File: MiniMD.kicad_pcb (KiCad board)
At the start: 2 copper layers, 100 x 100 mm, 82 parts, among them IC1 A3921KLPTR-T, IC2 SI4900DY-T1-E3, IC3 SI4900DY-T1-E3, IC4 A3921KLPTR-T, IC5 SI4900DY-T1-E3, IC6 SI4900DY-T1-E3, J1 Connector_Generic_Conn_01x05, J2 Connector_Generic_Conn_01x02, J3 Connector_Generic_Conn_01x02, J4 Connector_Generic_Conn_01x05, J5 Connector_Generic_Conn_01x02, J6 Connector_Generic_Conn_01x02, SW1 SW_Push, SW2 SW_Push, U1 FODM217A, U2 FODM217A, U3 FODM217A, U4 FODM217A, U5 FODM217A, U6 FODM217A, U7 FODM217A, U8 FODM217A

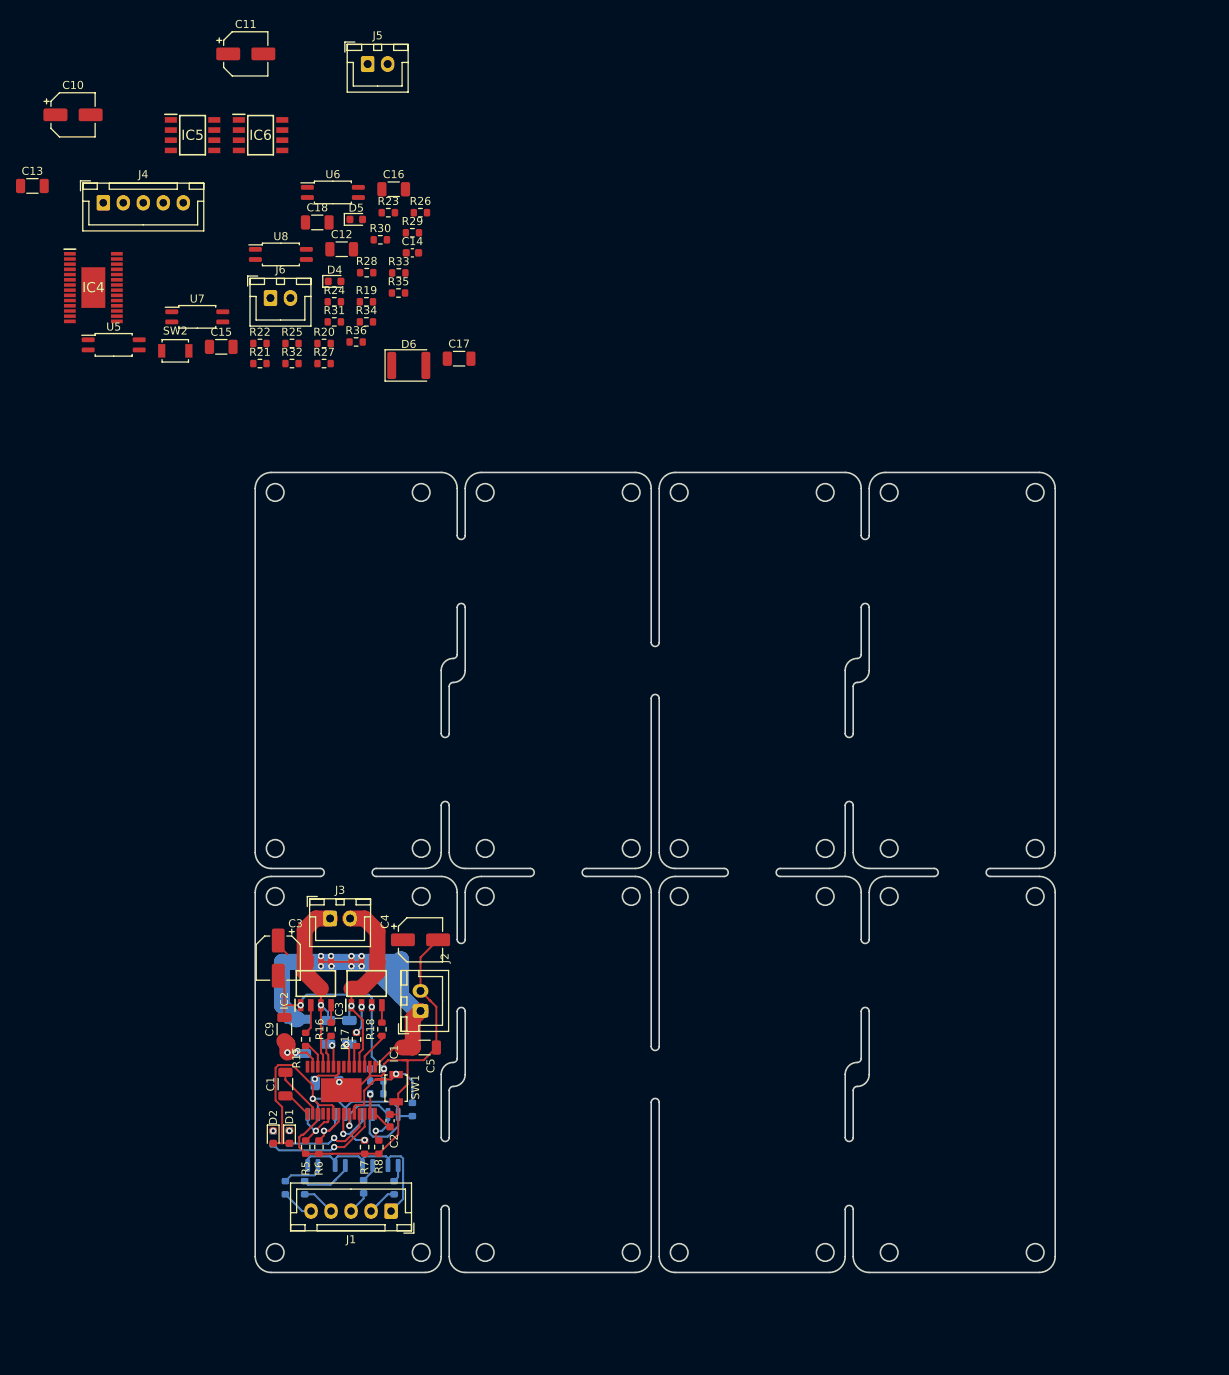
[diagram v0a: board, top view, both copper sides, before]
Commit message: シンボルの挿入まで完成
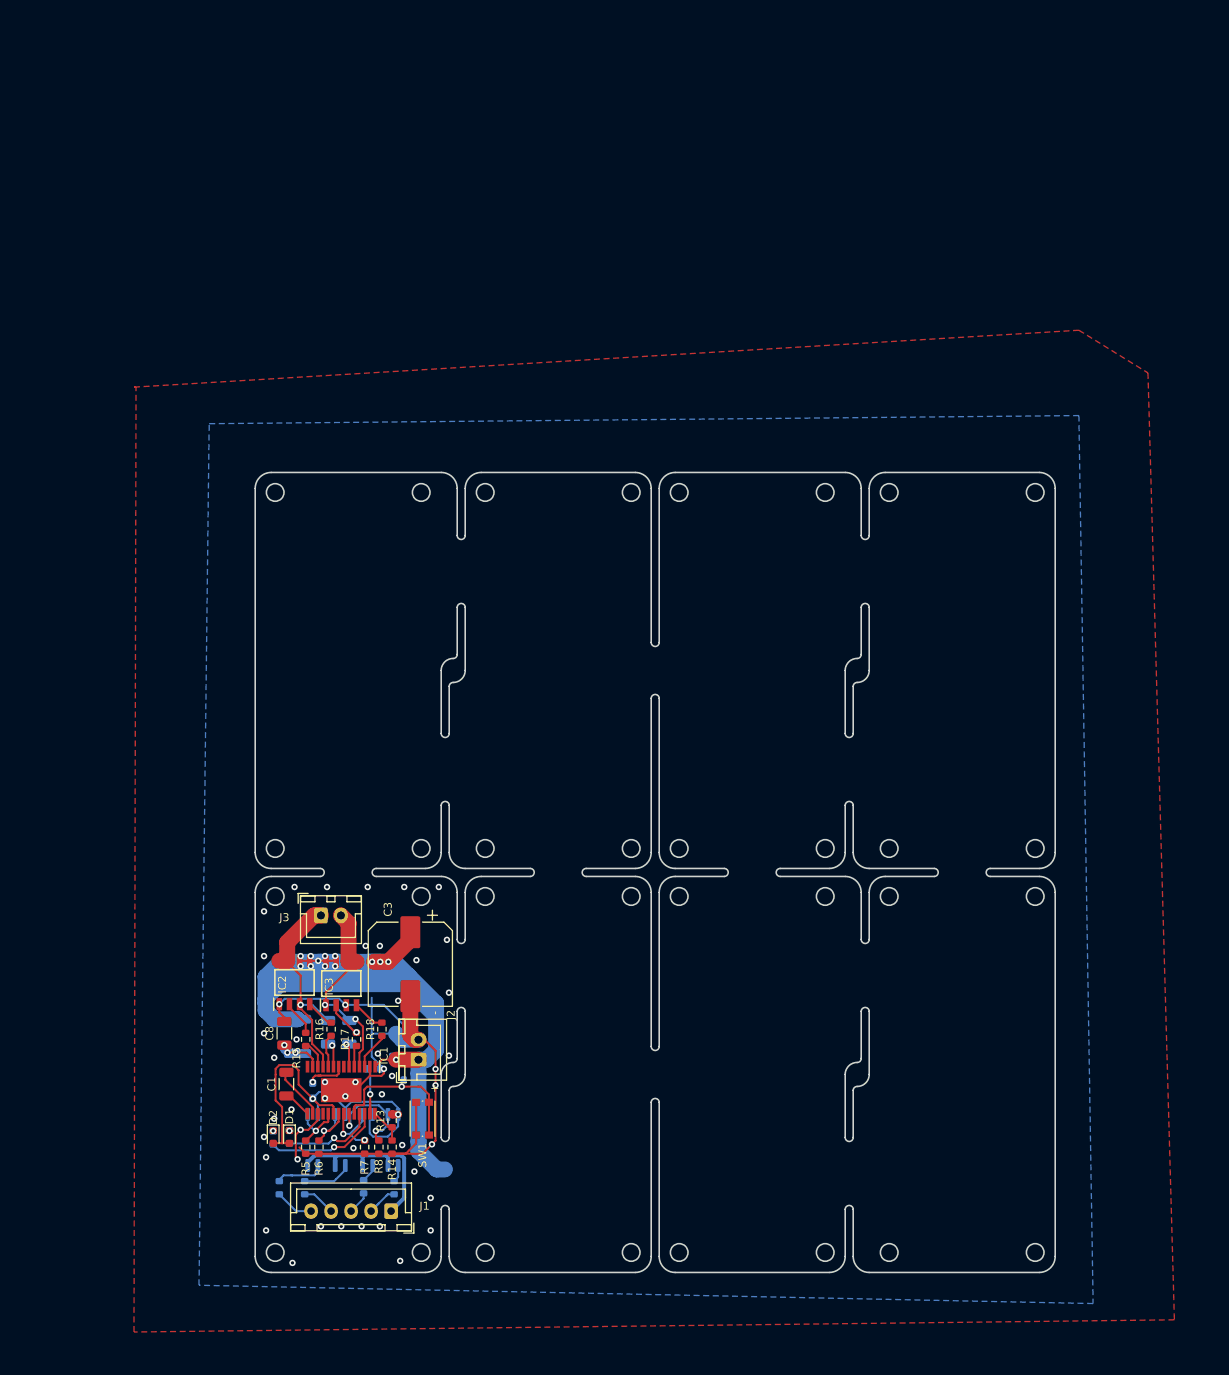
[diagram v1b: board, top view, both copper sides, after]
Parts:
- removed C10, C11: 220u, Capacitor_SMD:CP_Elec_5x3
- removed C12, C13, C17: 0.47u, Capacitor_SMD:C_1206_3216Metric
- removed C14: 0.1u, Capacitor_SMD:C_0603_1608Metric
- removed C15, C16, C18: 0.22u, Capacitor_SMD:C_1206_3216Metric
- removed the C4 at (173.0, 117.1)
- removed D4, D5: LED, LED_SMD:LED_0603_1608Metric
- removed D6: DIODE, Diode_SMD:D_1812_4532Metric
- removed IC4: A3921KLPTR-T, SamacSys_Parts:SOP65P640X120-29N
- removed IC5, IC6: SI4900DY-T1-E3, SamacSys_Parts:SOIC127P600X175-8N
- removed J4: Connector_Generic_Conn_01x05, Connector_JST:JST_XH_B5B-XH-A_1x05_P2.50mm_Vertical
- removed J5, J6: Connector_Generic_Conn_01x02, Connector_JST:JST_XH_B2B-XH-A_1x02_P2.50mm_Vertical
- removed R19, R20, R21, R22, R28, R29, R30, R31, R32: 1k, Resistor_SMD:R_0603_1608Metric
- removed R23, R24, R25, R26, R27: 10k, Resistor_SMD:R_0603_1608Metric
- removed R33, R34, R35, R36: 15, Resistor_SMD:R_0603_1608Metric
- removed SW2: SW_Push, Button_Switch_SMD:SW_SPST_B3U-1000P
- removed U5, U6, U7, U8: FODM217A, Package_SO:SOP-4_4.4x2.6mm_P1.27mm
- C2: value 0.1u -> 1u; moved to B.Cu
- C3: footprint Capacitor_SMD:CP_Elec_5x3 -> Capacitor_SMD:CP_Elec_10x10
- C4: renamed from C5; moved to B.Cu
- C7: renamed from C8; value 0.22u -> 1u; footprint Capacitor_SMD:C_1206_3216Metric -> Capacitor_SMD:C_0603_1608Metric
- R12: value 1k -> 100k
- R13: moved to F.Cu
- R14: value 1k -> 10k; moved to F.Cu
- SW1: value SW_Push -> SW_MEC_5G; footprint Button_Switch_SMD:SW_SPST_B3U-1000P -> Button_Switch_SMD:SW_Push_1P1T_NO_CK_KMR2
- moved C3 16.5 mm to (171.7, 120.1)
- moved C2 9.32 mm to (160.3, 136.9), turned to 0 degrees
- moved R14 6.93 mm to (169.4, 143.0), turned to 270 degrees
- moved J2 6.10 mm to (172.7, 132.1)
- moved R13 5.31 mm to (169.4, 139.7), turned to 90 degrees
- moved SW1 5.04 mm to (173.2, 139.4), turned to 270 degrees
- moved R9 3.69 mm to (171.7, 134.6), turned to 180 degrees
- moved C4 3.57 mm to (169.9, 130.3), turned to 90 degrees
- moved IC3 3.17 mm to (163.1, 122.6)
- moved IC2 2.67 mm to (157.2, 122.4)
- moved J3 1.20 mm to (160.5, 114.0)
- moved C7 1.02 mm to (160.3, 135.0)
- moved R1 0.76 mm to (155.3, 148.1)
- moved C8 0.51 mm to (156.0, 128.8)
- moved R12 0.38 mm to (167.1, 133.2)
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- renumbered C6 to C5, C7 to C6, C9 to C8
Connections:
- C2 pad 1: Net-(C2-Pad1) -> 5V_1
- IC1 pad 28: Net-(C2-Pad1) -> Net-(IC1-Pad28)
- R12 pad 1: Net-(R12-Pad1) -> Net-(IC1-Pad27)
- R13 pad 1: Net-(R12-Pad1) -> Net-(IC1-Pad28)
- R13 pad 2: Net-(R13-Pad2) -> 5V_1
- R14 pad 1: Net-(IC1-Pad27) -> Net-(IC1-Pad28)
- R14 pad 2: Net-(R13-Pad2) -> GND
- R9 pad 1: 5V_1 -> VCC
- SW1 pad 1: GND -> Net-(IC1-Pad24)
- SW1 pad 2: Net-(IC1-Pad24) -> GND
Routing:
- net VCC: track 63.8 -> 124.2 mm, vias 8 -> 13
- net GND: track 89.4 -> 100.8 mm, vias 4 -> 48
- net Net-(C5-Pad2): track 24.5 -> 29.1 mm
- net Net-(IC1-Pad28): track 0.00 -> 4.38 mm
- net Net-(IC1-Pad24): track 15.1 -> 18.8 mm
- net Net-(IC1-Pad27): track 3.88 -> 7.06 mm
- net Net-(C6-Pad2): track 28.5 -> 25.5 mm, vias 1 -> 2
- net Net-(C2-Pad1): track 2.73 -> 0.00 mm
- net Net-(IC3-Pad4): track 2.18 -> 4.08 mm
- net Net-(R13-Pad2): track 1.59 -> 0.00 mm
- net Net-(R12-Pad1): track 1.52 -> 0.00 mm
- net Net-(IC2-Pad4): track 2.18 -> 3.62 mm
- net GND1: track 25.6 -> 24.5 mm
- net Net-(IC3-Pad2): track 3.44 -> 4.56 mm, vias 2 -> 1
- net Net-(R1-Pad2): track 5.35 -> 6.36 mm
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- added copper zone on B.Cu, net GND
- added copper zone on F.Cu, net GND
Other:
- board text added: "+"
- board text added: "-"
- board text added: "GND"
- board text added: "PHASE"
- board text added: "PWMH"
- board text added: "PWML"
- board text added: "SR"
- board text added: "motor"

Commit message: 完成
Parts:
- removed the J1 at (169.3, 151.0)
- removed the R2 at (158.5, 148.1)
- removed the R4 at (169.7, 148.1)
- removed the U2 at (162.9, 142.1)
- removed U4: FODM217A, Package_SO:SOP-4_4.4x2.6mm_P1.27mm
- added C1: 220u, Capacitor_SMD:CP_Elec_10x10, F.Cu at (171.7, 69.6)
- added C1: 220u, Capacitor_SMD:CP_Elec_10x10, F.Cu at (182.5, 97.3)
- added C1: 220u, Capacitor_SMD:CP_Elec_10x10, F.Cu at (222.1, 69.6)
- added C1: 220u, Capacitor_SMD:CP_Elec_10x10, F.Cu at (232.9, 97.3)
- added C1: 220u, Capacitor_SMD:CP_Elec_10x10, F.Cu at (222.1, 120.1)
- added C1: 220u, Capacitor_SMD:CP_Elec_10x10, F.Cu at (232.9, 147.8)
- added C1: 220u, Capacitor_SMD:CP_Elec_10x10, F.Cu at (182.5, 147.8)
- added C2: 0.47u, Capacitor_SMD:C_1206_3216Metric, B.Cu at (169.9, 79.8)
- added C2: 0.47u, Capacitor_SMD:C_1206_3216Metric, B.Cu at (184.3, 87.1)
- added C2: 0.47u, Capacitor_SMD:C_1206_3216Metric, B.Cu at (220.3, 79.8)
- added C2: 0.47u, Capacitor_SMD:C_1206_3216Metric, B.Cu at (234.7, 87.1)
- added C2: 0.47u, Capacitor_SMD:C_1206_3216Metric, B.Cu at (220.3, 130.3)
- added C2: 0.47u, Capacitor_SMD:C_1206_3216Metric, B.Cu at (234.7, 137.7)
- added C2: 0.47u, Capacitor_SMD:C_1206_3216Metric, B.Cu at (184.3, 137.7)
- added C3: 0.47u, Capacitor_SMD:C_1206_3216Metric, F.Cu at (156.0, 78.2)
- added C3: 0.47u, Capacitor_SMD:C_1206_3216Metric, F.Cu at (198.2, 88.6)
- added C3: 0.47u, Capacitor_SMD:C_1206_3216Metric, F.Cu at (206.4, 78.2)
- added C3: 0.47u, Capacitor_SMD:C_1206_3216Metric, F.Cu at (248.7, 88.6)
- added C3: 0.47u, Capacitor_SMD:C_1206_3216Metric, F.Cu at (206.4, 128.8)
- added C3: 0.47u, Capacitor_SMD:C_1206_3216Metric, F.Cu at (248.7, 139.2)
- added C3: 0.47u, Capacitor_SMD:C_1206_3216Metric, F.Cu at (198.2, 139.2)
- added C4: 0.47u, Capacitor_SMD:C_1206_3216Metric, F.Cu at (156.2, 84.6)
- added C4: 0.47u, Capacitor_SMD:C_1206_3216Metric, F.Cu at (198.0, 82.3)
- added C4: 0.47u, Capacitor_SMD:C_1206_3216Metric, F.Cu at (206.6, 84.6)
- added C4: 0.47u, Capacitor_SMD:C_1206_3216Metric, F.Cu at (248.4, 82.3)
- added C4: 0.47u, Capacitor_SMD:C_1206_3216Metric, F.Cu at (206.6, 135.1)
- added C4: 0.47u, Capacitor_SMD:C_1206_3216Metric, F.Cu at (248.4, 132.8)
- added C4: 0.47u, Capacitor_SMD:C_1206_3216Metric, F.Cu at (198.0, 132.8)
- added C5: 0.47u, Capacitor_SMD:C_1206_3216Metric, B.Cu at (161.4, 78.1)
- added C5: 0.47u, Capacitor_SMD:C_1206_3216Metric, B.Cu at (192.8, 88.8)
- added C5: 0.47u, Capacitor_SMD:C_1206_3216Metric, B.Cu at (211.8, 78.1)
- added C5: 0.47u, Capacitor_SMD:C_1206_3216Metric, B.Cu at (243.2, 88.8)
- added C5: 0.47u, Capacitor_SMD:C_1206_3216Metric, B.Cu at (211.8, 128.7)
- added C5: 0.47u, Capacitor_SMD:C_1206_3216Metric, B.Cu at (243.2, 139.3)
- added C5: 0.47u, Capacitor_SMD:C_1206_3216Metric, B.Cu at (192.8, 139.3)
- added C6: 0.47u, Capacitor_SMD:C_1206_3216Metric, B.Cu at (190.1, 88.8)
- added C6: 0.47u, Capacitor_SMD:C_1206_3216Metric, B.Cu at (164.1, 78.1)
- added C6: 0.47u, Capacitor_SMD:C_1206_3216Metric, B.Cu at (240.5, 88.8)
- added C6: 0.47u, Capacitor_SMD:C_1206_3216Metric, B.Cu at (214.5, 78.1)
- added C6: 0.47u, Capacitor_SMD:C_1206_3216Metric, B.Cu at (214.5, 128.7)
- added C6: 0.47u, Capacitor_SMD:C_1206_3216Metric, B.Cu at (240.5, 139.3)
- added C6: 0.47u, Capacitor_SMD:C_1206_3216Metric, B.Cu at (190.1, 139.3)
- added C7: 1u, Capacitor_SMD:C_0603_1608Metric, B.Cu at (160.3, 84.5)
- added C7: 1u, Capacitor_SMD:C_0603_1608Metric, B.Cu at (193.9, 82.4)
- added C7: 1u, Capacitor_SMD:C_0603_1608Metric, B.Cu at (210.7, 84.5)
- added C7: 1u, Capacitor_SMD:C_0603_1608Metric, B.Cu at (244.3, 82.4)
- added C7: 1u, Capacitor_SMD:C_0603_1608Metric, B.Cu at (210.7, 135.0)
- added C7: 1u, Capacitor_SMD:C_0603_1608Metric, B.Cu at (244.3, 133.0)
- added C7: 1u, Capacitor_SMD:C_0603_1608Metric, B.Cu at (193.9, 133.0)
- added C8: 1u, Capacitor_SMD:C_0603_1608Metric, B.Cu at (160.3, 86.4)
- added C8: 1u, Capacitor_SMD:C_0603_1608Metric, B.Cu at (193.9, 80.5)
- added C8: 1u, Capacitor_SMD:C_0603_1608Metric, B.Cu at (210.7, 86.4)
- added C8: 1u, Capacitor_SMD:C_0603_1608Metric, B.Cu at (244.3, 80.5)
- added C8: 1u, Capacitor_SMD:C_0603_1608Metric, B.Cu at (210.7, 136.9)
- added C8: 1u, Capacitor_SMD:C_0603_1608Metric, B.Cu at (244.3, 131.1)
- added C8: 1u, Capacitor_SMD:C_0603_1608Metric, B.Cu at (193.9, 131.1)
- added D1: DIODE, Diode_SMD:D_1812_4532Metric, B.Cu at (157.6, 78.6)
- added D1: DIODE, Diode_SMD:D_1812_4532Metric, B.Cu at (196.6, 88.3)
- added D1: DIODE, Diode_SMD:D_1812_4532Metric, B.Cu at (208.0, 78.6)
- added D1: DIODE, Diode_SMD:D_1812_4532Metric, B.Cu at (247.0, 88.3)
- added D1: DIODE, Diode_SMD:D_1812_4532Metric, B.Cu at (208.0, 129.2)
- added D1: DIODE, Diode_SMD:D_1812_4532Metric, B.Cu at (247.0, 138.8)
- added D1: DIODE, Diode_SMD:D_1812_4532Metric, B.Cu at (196.6, 138.8)
- added D2: LED, LED_SMD:LED_0603_1608Metric, F.Cu at (156.6, 91.2)
- added D2: LED, LED_SMD:LED_0603_1608Metric, F.Cu at (197.6, 75.7)
- added D2: LED, LED_SMD:LED_0603_1608Metric, F.Cu at (207.0, 91.2)
- added D2: LED, LED_SMD:LED_0603_1608Metric, F.Cu at (248.0, 75.7)
- added D2: LED, LED_SMD:LED_0603_1608Metric, F.Cu at (207.0, 141.7)
- added D2: LED, LED_SMD:LED_0603_1608Metric, F.Cu at (248.0, 126.2)
- added D2: LED, LED_SMD:LED_0603_1608Metric, F.Cu at (197.6, 126.2)
- added D3: LED, LED_SMD:LED_0603_1608Metric, F.Cu at (154.6, 91.2)
- added D3: LED, LED_SMD:LED_0603_1608Metric, F.Cu at (199.6, 75.7)
- added D3: LED, LED_SMD:LED_0603_1608Metric, F.Cu at (205.0, 91.2)
- added D3: LED, LED_SMD:LED_0603_1608Metric, F.Cu at (250.1, 75.7)
- added D3: LED, LED_SMD:LED_0603_1608Metric, F.Cu at (205.0, 141.7)
- added D3: LED, LED_SMD:LED_0603_1608Metric, F.Cu at (250.1, 126.2)
- added D3: LED, LED_SMD:LED_0603_1608Metric, F.Cu at (199.6, 126.2)
- added G***: LOGO, MyLibrary:my_symbol_m, B.Cu at (171.7, 93.0)
- added G***: LOGO, MyLibrary:my_symbol_m, B.Cu at (182.5, 73.9)
- added G***: LOGO, MyLibrary:my_symbol_m, B.Cu at (222.1, 93.0)
- added G***: LOGO, MyLibrary:my_symbol_m, B.Cu at (232.9, 73.9)
- added G***: LOGO, MyLibrary:my_symbol_m, B.Cu at (222.1, 143.5)
- added G***: LOGO, MyLibrary:my_symbol_m, B.Cu at (232.9, 124.5)
- added G***: LOGO, MyLibrary:my_symbol_m, B.Cu at (182.5, 124.5)
- added G***: LOGO, MyLibrary:my_symbol_m, B.Cu at (171.7, 143.5)
- added IC1: SI4900DY-T1-E3, SamacSys_Parts:SOIC127P600X175-8N, F.Cu at (197.0, 145.5)
- added IC1: SI4900DY-T1-E3, SamacSys_Parts:SOIC127P600X175-8N, F.Cu at (207.6, 122.4)
- added IC1: SI4900DY-T1-E3, SamacSys_Parts:SOIC127P600X175-8N, F.Cu at (247.4, 145.5)
- added IC1: SI4900DY-T1-E3, SamacSys_Parts:SOIC127P600X175-8N, F.Cu at (247.4, 95.0)
- added IC1: SI4900DY-T1-E3, SamacSys_Parts:SOIC127P600X175-8N, F.Cu at (207.6, 71.9)
- added IC1: SI4900DY-T1-E3, SamacSys_Parts:SOIC127P600X175-8N, F.Cu at (197.0, 95.0)
- added IC1: SI4900DY-T1-E3, SamacSys_Parts:SOIC127P600X175-8N, F.Cu at (157.2, 71.9)
- added IC2: SI4900DY-T1-E3, SamacSys_Parts:SOIC127P600X175-8N, F.Cu at (191.1, 145.4)
- added IC2: SI4900DY-T1-E3, SamacSys_Parts:SOIC127P600X175-8N, F.Cu at (213.5, 122.6)
- added IC2: SI4900DY-T1-E3, SamacSys_Parts:SOIC127P600X175-8N, F.Cu at (241.6, 145.4)
- added IC2: SI4900DY-T1-E3, SamacSys_Parts:SOIC127P600X175-8N, F.Cu at (241.6, 94.9)
- added IC2: SI4900DY-T1-E3, SamacSys_Parts:SOIC127P600X175-8N, F.Cu at (213.5, 72.0)
- added IC2: SI4900DY-T1-E3, SamacSys_Parts:SOIC127P600X175-8N, F.Cu at (191.1, 94.9)
- added IC2: SI4900DY-T1-E3, SamacSys_Parts:SOIC127P600X175-8N, F.Cu at (163.1, 72.0)
- added IC3: A3921KLPTR-T, SamacSys_Parts:SOP65P640X120-29N, F.Cu at (191.1, 132.1)
- added IC3: A3921KLPTR-T, SamacSys_Parts:SOP65P640X120-29N, F.Cu at (213.5, 135.9)
- added IC3: A3921KLPTR-T, SamacSys_Parts:SOP65P640X120-29N, F.Cu at (241.6, 132.1)
- added IC3: A3921KLPTR-T, SamacSys_Parts:SOP65P640X120-29N, F.Cu at (241.6, 81.5)
- added IC3: A3921KLPTR-T, SamacSys_Parts:SOP65P640X120-29N, F.Cu at (213.5, 85.3)
- added IC3: A3921KLPTR-T, SamacSys_Parts:SOP65P640X120-29N, F.Cu at (191.1, 81.5)
- added IC3: A3921KLPTR-T, SamacSys_Parts:SOP65P640X120-29N, F.Cu at (163.1, 85.3)
- added J1: Connector_Generic_Conn_01x02, Connector_JST:JST_XH_B2B-XH-A_1x02_P2.50mm_Vertical, F.Cu at (172.7, 81.5)
- added J1: Connector_Generic_Conn_01x02, Connector_JST:JST_XH_B2B-XH-A_1x02_P2.50mm_Vertical, F.Cu at (181.5, 85.3)
- added J1: Connector_Generic_Conn_01x02, Connector_JST:JST_XH_B2B-XH-A_1x02_P2.50mm_Vertical, F.Cu at (223.1, 81.5)
- added J1: Connector_Generic_Conn_01x02, Connector_JST:JST_XH_B2B-XH-A_1x02_P2.50mm_Vertical, F.Cu at (231.9, 85.3)
- added J1: Connector_Generic_Conn_01x02, Connector_JST:JST_XH_B2B-XH-A_1x02_P2.50mm_Vertical, F.Cu at (223.1, 132.1)
- added J1: Connector_Generic_Conn_01x02, Connector_JST:JST_XH_B2B-XH-A_1x02_P2.50mm_Vertical, F.Cu at (231.9, 135.9)
- added J1: Connector_Generic_Conn_01x02, Connector_JST:JST_XH_B2B-XH-A_1x02_P2.50mm_Vertical, F.Cu at (181.5, 135.9)
- added J2: Conn_01x03, Connector_JST:JST_XH_B3B-XH-A_1x03_P2.50mm_Vertical, F.Cu at (162.0, 100.5)
- added J2: Conn_01x03, Connector_JST:JST_XH_B3B-XH-A_1x03_P2.50mm_Vertical, F.Cu at (192.2, 66.4)
- added J2: Conn_01x03, Connector_JST:JST_XH_B3B-XH-A_1x03_P2.50mm_Vertical, F.Cu at (212.4, 100.5)
- added J2: Conn_01x03, Connector_JST:JST_XH_B3B-XH-A_1x03_P2.50mm_Vertical, F.Cu at (242.6, 66.4)
- added J2: Conn_01x03, Connector_JST:JST_XH_B3B-XH-A_1x03_P2.50mm_Vertical, F.Cu at (212.4, 151.0)
- added J2: Conn_01x03, Connector_JST:JST_XH_B3B-XH-A_1x03_P2.50mm_Vertical, F.Cu at (242.6, 117.0)
- added J2: Conn_01x03, Connector_JST:JST_XH_B3B-XH-A_1x03_P2.50mm_Vertical, F.Cu at (192.2, 117.0)
- added J2: Conn_01x03, Connector_JST:JST_XH_B3B-XH-A_1x03_P2.50mm_Vertical, F.Cu at (162.0, 151.0)
- added J3: Connector_Generic_Conn_01x02, Connector_JST:JST_XH_B2B-XH-A_1x02_P2.50mm_Vertical, F.Cu at (191.0, 103.3)
- added J3: Connector_Generic_Conn_01x02, Connector_JST:JST_XH_B2B-XH-A_1x02_P2.50mm_Vertical, F.Cu at (163.2, 63.6)
- added J3: Connector_Generic_Conn_01x02, Connector_JST:JST_XH_B2B-XH-A_1x02_P2.50mm_Vertical, F.Cu at (213.6, 63.6)
- added J3: Connector_Generic_Conn_01x02, Connector_JST:JST_XH_B2B-XH-A_1x02_P2.50mm_Vertical, F.Cu at (241.4, 103.3)
- added J3: Connector_Generic_Conn_01x02, Connector_JST:JST_XH_B2B-XH-A_1x02_P2.50mm_Vertical, F.Cu at (213.6, 114.2)
- added J3: Connector_Generic_Conn_01x02, Connector_JST:JST_XH_B2B-XH-A_1x02_P2.50mm_Vertical, F.Cu at (241.4, 153.8)
- added J3: Connector_Generic_Conn_01x02, Connector_JST:JST_XH_B2B-XH-A_1x02_P2.50mm_Vertical, F.Cu at (191.0, 153.8)
- added R1: 10k, Resistor_SMD:R_0603_1608Metric, B.Cu at (171.7, 84.1)
- added R1: 10k, Resistor_SMD:R_0603_1608Metric, B.Cu at (182.5, 82.8)
- added R1: 10k, Resistor_SMD:R_0603_1608Metric, B.Cu at (222.1, 84.1)
- added R1: 10k, Resistor_SMD:R_0603_1608Metric, B.Cu at (232.9, 82.8)
- added R1: 10k, Resistor_SMD:R_0603_1608Metric, B.Cu at (222.1, 134.6)
- added R1: 10k, Resistor_SMD:R_0603_1608Metric, B.Cu at (232.9, 133.3)
- added R1: 10k, Resistor_SMD:R_0603_1608Metric, B.Cu at (182.5, 133.3)
- added R10: 10k, Resistor_SMD:R_0603_1608Metric, F.Cu at (166.0, 92.5)
- added R10: 10k, Resistor_SMD:R_0603_1608Metric, F.Cu at (188.2, 74.4)
- added R10: 10k, Resistor_SMD:R_0603_1608Metric, F.Cu at (216.4, 92.5)
- added R10: 10k, Resistor_SMD:R_0603_1608Metric, F.Cu at (238.6, 74.4)
- added R10: 10k, Resistor_SMD:R_0603_1608Metric, F.Cu at (216.4, 143.0)
- added R10: 10k, Resistor_SMD:R_0603_1608Metric, F.Cu at (238.6, 125.0)
- added R10: 10k, Resistor_SMD:R_0603_1608Metric, F.Cu at (188.2, 125.0)
- added R11: 47, Resistor_SMD:R_0603_1608Metric, F.Cu at (168.1, 77.7)
- added R11: 47, Resistor_SMD:R_0603_1608Metric, F.Cu at (186.1, 89.2)
- added R11: 47, Resistor_SMD:R_0603_1608Metric, F.Cu at (218.6, 77.7)
- added R11: 47, Resistor_SMD:R_0603_1608Metric, F.Cu at (236.5, 89.2)
- added R11: 47, Resistor_SMD:R_0603_1608Metric, F.Cu at (218.6, 128.3)
- added R11: 47, Resistor_SMD:R_0603_1608Metric, F.Cu at (236.5, 139.7)
- added R11: 47, Resistor_SMD:R_0603_1608Metric, F.Cu at (186.1, 139.7)
- added R12: 1k, Resistor_SMD:R_0603_1608Metric, B.Cu at (156.6, 91.2)
- added R12: 1k, Resistor_SMD:R_0603_1608Metric, B.Cu at (197.6, 75.7)
- added R12: 1k, Resistor_SMD:R_0603_1608Metric, B.Cu at (207.0, 91.2)
- added R12: 1k, Resistor_SMD:R_0603_1608Metric, B.Cu at (248.0, 75.7)
- added R12: 1k, Resistor_SMD:R_0603_1608Metric, B.Cu at (207.0, 141.7)
- added R12: 1k, Resistor_SMD:R_0603_1608Metric, B.Cu at (248.0, 126.2)
- added R12: 1k, Resistor_SMD:R_0603_1608Metric, B.Cu at (197.6, 126.2)
- added R13: 1k, Resistor_SMD:R_0603_1608Metric, B.Cu at (154.6, 91.3)
- added R13: 1k, Resistor_SMD:R_0603_1608Metric, B.Cu at (199.6, 75.6)
- added R13: 1k, Resistor_SMD:R_0603_1608Metric, B.Cu at (205.0, 91.3)
- added R13: 1k, Resistor_SMD:R_0603_1608Metric, B.Cu at (250.1, 75.6)
- added R13: 1k, Resistor_SMD:R_0603_1608Metric, B.Cu at (205.0, 141.9)
- added R13: 1k, Resistor_SMD:R_0603_1608Metric, B.Cu at (250.1, 126.1)
- added R13: 1k, Resistor_SMD:R_0603_1608Metric, B.Cu at (199.6, 126.1)
- added R14: 100k, Resistor_SMD:R_0603_1608Metric, B.Cu at (167.1, 82.7)
- added R14: 100k, Resistor_SMD:R_0603_1608Metric, B.Cu at (187.1, 84.2)
- added R14: 100k, Resistor_SMD:R_0603_1608Metric, B.Cu at (217.6, 82.7)
- added R14: 100k, Resistor_SMD:R_0603_1608Metric, B.Cu at (237.5, 84.2)
- added R14: 100k, Resistor_SMD:R_0603_1608Metric, B.Cu at (217.6, 133.2)
- added R14: 100k, Resistor_SMD:R_0603_1608Metric, B.Cu at (237.5, 134.7)
- added R14: 100k, Resistor_SMD:R_0603_1608Metric, B.Cu at (187.1, 134.7)
- added R15: 1k, Resistor_SMD:R_0603_1608Metric, F.Cu at (169.4, 89.2)
- added R15: 1k, Resistor_SMD:R_0603_1608Metric, F.Cu at (184.8, 77.7)
- added R15: 1k, Resistor_SMD:R_0603_1608Metric, F.Cu at (219.8, 89.2)
- added R15: 1k, Resistor_SMD:R_0603_1608Metric, F.Cu at (235.2, 77.7)
- added R15: 1k, Resistor_SMD:R_0603_1608Metric, F.Cu at (219.8, 139.7)
- added R15: 1k, Resistor_SMD:R_0603_1608Metric, F.Cu at (235.2, 128.3)
- added R15: 1k, Resistor_SMD:R_0603_1608Metric, F.Cu at (184.8, 128.3)
- added R16: 10k, Resistor_SMD:R_0603_1608Metric, F.Cu at (184.8, 74.4)
- added R16: 10k, Resistor_SMD:R_0603_1608Metric, F.Cu at (169.4, 92.5)
- added R16: 10k, Resistor_SMD:R_0603_1608Metric, F.Cu at (219.8, 92.5)
- added R16: 10k, Resistor_SMD:R_0603_1608Metric, F.Cu at (235.2, 74.4)
- added R16: 10k, Resistor_SMD:R_0603_1608Metric, F.Cu at (219.8, 143.0)
- added R16: 10k, Resistor_SMD:R_0603_1608Metric, F.Cu at (235.2, 125.0)
- added R16: 10k, Resistor_SMD:R_0603_1608Metric, F.Cu at (184.8, 125.0)
- added R2: 10k, Resistor_SMD:R_0603_1608Metric, F.Cu at (160.3, 92.5)
- added R2: 10k, Resistor_SMD:R_0603_1608Metric, F.Cu at (193.9, 74.4)
- added R2: 10k, Resistor_SMD:R_0603_1608Metric, F.Cu at (210.7, 92.5)
- added R2: 10k, Resistor_SMD:R_0603_1608Metric, F.Cu at (244.3, 74.4)
- added R2: 10k, Resistor_SMD:R_0603_1608Metric, F.Cu at (210.7, 143.0)
- added R2: 10k, Resistor_SMD:R_0603_1608Metric, F.Cu at (244.3, 125.0)
- added R2: 10k, Resistor_SMD:R_0603_1608Metric, F.Cu at (193.9, 125.0)
- added R3: 10k, Resistor_SMD:R_0603_1608Metric, F.Cu at (186.4, 74.4)
- added R3: 10k, Resistor_SMD:R_0603_1608Metric, F.Cu at (167.8, 92.5)
- added R3: 10k, Resistor_SMD:R_0603_1608Metric, F.Cu at (236.9, 74.4)
- added R3: 10k, Resistor_SMD:R_0603_1608Metric, F.Cu at (218.2, 92.5)
- added R3: 10k, Resistor_SMD:R_0603_1608Metric, F.Cu at (218.2, 143.0)
- added R3: 10k, Resistor_SMD:R_0603_1608Metric, F.Cu at (236.9, 125.0)
- added R3: 10k, Resistor_SMD:R_0603_1608Metric, F.Cu at (186.4, 125.0)
- added R4: 1k, Resistor_SMD:R_0603_1608Metric, B.Cu at (158.1, 98.2)
- added R4: 1k, Resistor_SMD:R_0603_1608Metric, B.Cu at (196.1, 68.7)
- added R4: 1k, Resistor_SMD:R_0603_1608Metric, B.Cu at (208.5, 98.2)
- added R4: 1k, Resistor_SMD:R_0603_1608Metric, B.Cu at (246.5, 68.7)
- added R4: 1k, Resistor_SMD:R_0603_1608Metric, B.Cu at (208.5, 148.7)
- added R4: 1k, Resistor_SMD:R_0603_1608Metric, B.Cu at (246.5, 119.3)
- added R4: 1k, Resistor_SMD:R_0603_1608Metric, B.Cu at (196.1, 119.3)
- added R5: 47, Resistor_SMD:R_0603_1608Metric, F.Cu at (158.6, 79.0)
- added R5: 47, Resistor_SMD:R_0603_1608Metric, F.Cu at (195.6, 87.9)
- added R5: 47, Resistor_SMD:R_0603_1608Metric, F.Cu at (209.0, 79.0)
- added R5: 47, Resistor_SMD:R_0603_1608Metric, F.Cu at (246.0, 87.9)
- added R5: 47, Resistor_SMD:R_0603_1608Metric, F.Cu at (209.0, 129.5)
- added R5: 47, Resistor_SMD:R_0603_1608Metric, F.Cu at (246.0, 138.4)
- added R5: 47, Resistor_SMD:R_0603_1608Metric, F.Cu at (195.6, 138.4)
- added R6: 47, Resistor_SMD:R_0603_1608Metric, F.Cu at (161.8, 77.7)
- added R6: 47, Resistor_SMD:R_0603_1608Metric, F.Cu at (192.4, 89.2)
- added R6: 47, Resistor_SMD:R_0603_1608Metric, F.Cu at (212.2, 77.7)
- added R6: 47, Resistor_SMD:R_0603_1608Metric, F.Cu at (242.8, 89.2)
- added R6: 47, Resistor_SMD:R_0603_1608Metric, F.Cu at (212.2, 128.3)
- added R6: 47, Resistor_SMD:R_0603_1608Metric, F.Cu at (242.8, 139.7)
- added R6: 47, Resistor_SMD:R_0603_1608Metric, F.Cu at (192.4, 139.7)
- added R7: 1k, Resistor_SMD:R_0603_1608Metric, B.Cu at (165.9, 97.4)
- added R7: 1k, Resistor_SMD:R_0603_1608Metric, B.Cu at (188.3, 69.5)
- added R7: 1k, Resistor_SMD:R_0603_1608Metric, B.Cu at (216.3, 97.4)
- added R7: 1k, Resistor_SMD:R_0603_1608Metric, B.Cu at (238.8, 69.5)
- added R7: 1k, Resistor_SMD:R_0603_1608Metric, B.Cu at (216.3, 148.0)
- added R7: 1k, Resistor_SMD:R_0603_1608Metric, B.Cu at (238.8, 120.0)
- added R7: 1k, Resistor_SMD:R_0603_1608Metric, B.Cu at (188.3, 120.0)
- added R8: 47, Resistor_SMD:R_0603_1608Metric, F.Cu at (165.0, 79.0)
- added R8: 47, Resistor_SMD:R_0603_1608Metric, F.Cu at (189.2, 87.9)
- added R8: 47, Resistor_SMD:R_0603_1608Metric, F.Cu at (215.4, 79.0)
- added R8: 47, Resistor_SMD:R_0603_1608Metric, F.Cu at (239.6, 87.9)
- added R8: 47, Resistor_SMD:R_0603_1608Metric, F.Cu at (215.4, 129.5)
- added R8: 47, Resistor_SMD:R_0603_1608Metric, F.Cu at (239.6, 138.4)
- added R8: 47, Resistor_SMD:R_0603_1608Metric, F.Cu at (189.2, 138.4)
- added R9: 10k, Resistor_SMD:R_0603_1608Metric, F.Cu at (158.6, 92.5)
- added R9: 10k, Resistor_SMD:R_0603_1608Metric, F.Cu at (195.6, 74.4)
- added R9: 10k, Resistor_SMD:R_0603_1608Metric, F.Cu at (209.0, 92.5)
- added R9: 10k, Resistor_SMD:R_0603_1608Metric, F.Cu at (246.0, 74.4)
- added R9: 10k, Resistor_SMD:R_0603_1608Metric, F.Cu at (209.0, 143.0)
- added R9: 10k, Resistor_SMD:R_0603_1608Metric, F.Cu at (246.0, 125.0)
- added R9: 10k, Resistor_SMD:R_0603_1608Metric, F.Cu at (195.6, 125.0)
- added SW1: SW_MEC_5G, Button_Switch_SMD:SW_Push_1P1T_NO_CK_KMR2, F.Cu at (181.0, 78.0)
- added SW1: SW_MEC_5G, Button_Switch_SMD:SW_Push_1P1T_NO_CK_KMR2, F.Cu at (173.2, 88.9)
- added SW1: SW_MEC_5G, Button_Switch_SMD:SW_Push_1P1T_NO_CK_KMR2, F.Cu at (231.4, 78.0)
- added SW1: SW_MEC_5G, Button_Switch_SMD:SW_Push_1P1T_NO_CK_KMR2, F.Cu at (223.6, 88.9)
- added SW1: SW_MEC_5G, Button_Switch_SMD:SW_Push_1P1T_NO_CK_KMR2, F.Cu at (223.6, 139.4)
- added SW1: SW_MEC_5G, Button_Switch_SMD:SW_Push_1P1T_NO_CK_KMR2, F.Cu at (231.4, 128.5)
- added SW1: SW_MEC_5G, Button_Switch_SMD:SW_Push_1P1T_NO_CK_KMR2, F.Cu at (181.0, 128.5)
- added U1: FODM217A, Package_SO:SOP-4_4.4x2.6mm_P1.27mm, B.Cu at (194.7, 75.3)
- added U1: FODM217A, Package_SO:SOP-4_4.4x2.6mm_P1.27mm, B.Cu at (159.5, 91.6)
- added U1: FODM217A, Package_SO:SOP-4_4.4x2.6mm_P1.27mm, B.Cu at (245.1, 75.3)
- added U1: FODM217A, Package_SO:SOP-4_4.4x2.6mm_P1.27mm, B.Cu at (209.9, 91.6)
- added U1: FODM217A, Package_SO:SOP-4_4.4x2.6mm_P1.27mm, B.Cu at (209.9, 142.1)
- added U1: FODM217A, Package_SO:SOP-4_4.4x2.6mm_P1.27mm, B.Cu at (245.1, 125.9)
- added U1: FODM217A, Package_SO:SOP-4_4.4x2.6mm_P1.27mm, B.Cu at (194.7, 125.9)
- added U2: FODM217A, Package_SO:SOP-4_4.4x2.6mm_P1.27mm, B.Cu at (166.4, 91.6)
- added U2: FODM217A, Package_SO:SOP-4_4.4x2.6mm_P1.27mm, B.Cu at (187.8, 75.3)
- added U2: FODM217A, Package_SO:SOP-4_4.4x2.6mm_P1.27mm, B.Cu at (216.8, 91.6)
- added U2: FODM217A, Package_SO:SOP-4_4.4x2.6mm_P1.27mm, B.Cu at (238.3, 75.3)
- added U2: FODM217A, Package_SO:SOP-4_4.4x2.6mm_P1.27mm, B.Cu at (216.8, 142.1)
- added U2: FODM217A, Package_SO:SOP-4_4.4x2.6mm_P1.27mm, B.Cu at (238.3, 125.9)
- added U2: FODM217A, Package_SO:SOP-4_4.4x2.6mm_P1.27mm, B.Cu at (187.8, 125.9)
- C5, C6: value 0.22u -> 0.47u
- moved R4 2.87 mm to (158.1, 148.7)
- moved J3 2.67 mm to (163.2, 114.2), turned to 180 degrees
- turned R3 to 90 degrees
- renumbered C3 to C1, C4 to C2, C8 to C3, C1 to C4, C2 to C8, D3 to D1, D1 to D2, D2 to D3, IC2 to IC1, IC3 to IC2, IC1 to IC3, J2 to J1, R9 to R1, R7 to R10, R18 to R11, R10 to R12, R11 to R13, R12 to R14, R13 to R15, R14 to R16, R6 to R2, R8 to R3, R1 to R4, R15 to R5, R16 to R6, R3 to R7, R17 to R8, R5 to R9, U3 to U2
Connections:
- IC3 pad 21: Net-(IC1-Pad21) -> Net-(IC3-Pad21)
- IC3 pad 23: Net-(IC1-Pad23) -> Net-(IC3-Pad23)
- J3 pad 1: Net-(C5-Pad2) -> Net-(C6-Pad2)
- J3 pad 2: Net-(C6-Pad2) -> Net-(C5-Pad2)
- R2 pad 1: Net-(IC1-Pad21) -> 5V_1
- R2 pad 2: GND -> Net-(IC3-Pad21)
- R3 pad 1: Net-(IC1-Pad23) -> 5V_1
- R3 pad 2: GND -> Net-(IC3-Pad23)
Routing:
- net VCC: track 124.2 -> 1045.9 mm, vias 13 -> 104
- net GND: track 100.8 -> 634.7 mm, vias 48 -> 368
- net 5V_1: track 50.1 -> 435.7 mm, vias 2 -> 16
- net Net-(C5-Pad2): track 29.1 -> 234.0 mm, vias 1 -> 8
- net Net-(C6-Pad2): track 25.5 -> 202.1 mm, vias 2 -> 16
- net Net-(IC3-Pad24): track 18.8 -> 153.2 mm, vias 1 -> 8
- net GND1: track 24.5 -> 130.3 mm
- net Net-(IC3-Pad23): track 0.00 -> 105.5 mm, vias 0 -> 16
- net Net-(IC3-Pad26): track 14.6 -> 116.7 mm, vias 1 -> 8
- net Net-(IC3-Pad25): track 11.7 -> 93.4 mm, vias 1 -> 8
- net Net-(J2-Pad3): track 4.88 -> 85.4 mm
- net Net-(IC3-Pad22): track 8.62 -> 69.0 mm, vias 2 -> 16
- net Net-(IC3-Pad19): track 7.23 -> 57.9 mm, vias 1 -> 8
- net Net-(IC3-Pad27): track 7.06 -> 56.5 mm, vias 1 -> 8
- net Net-(IC3-Pad21): track 0.00 -> 48.2 mm
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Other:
- board text added: "Designed by Akutagawa 2021/06/02"
- board text added: "MiniMD Ver1"
- board text removed: "PWMH"
- board text removed: "SR"
